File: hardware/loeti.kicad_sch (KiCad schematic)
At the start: 101 parts, among them J1 REDFIT_SWD_6, J2 POWER, J3 DEBUG, Q1 Si4162DY, Q2 BC817, Q3 Si4425FDY, Q4 BC817, Q5 BC807, SW1 BOOT, SW3 RotaryEncoder_Switch, U10 TPS62177DQC, U2 EA_OLEDS102-6, U3 M24C64-RMN, U4 STM32G431CBTx, U5 TCPP01-M12, U6 74AHC1G08, U7 USBLC6-2SC6, U8 TLV333-DBV, U9 INA301A1

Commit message: chore: update PCB design
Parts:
- removed D3: BAT54S, Package_TO_SOT_SMD:SOT-23, symbol Diode:BAT54S
- removed R10, R8: 10k, Resistor_SMD:R_0603_1608Metric, symbol Device:R
- removed TP1: 1C, Connector_Wire:SolderWire-0.75sqmm_1x01_D1.25mm_OD2.3mm, symbol Connector:TestPoint
- removed TP2: 3P, Connector_Wire:SolderWire-0.75sqmm_1x01_D1.25mm_OD2.3mm, symbol Connector:TestPoint
- removed TP3: 2T, Connector_Wire:SolderWire-0.75sqmm_1x01_D1.25mm_OD2.3mm, symbol Connector:TestPoint
- removed TP4: 4D, Connector_Wire:SolderWire-0.75sqmm_1x01_D1.25mm_OD2.3mm, symbol Connector:TestPoint
- removed TP5: 5S, Connector_Wire:SolderWire-0.75sqmm_1x01_D1.25mm_OD2.3mm, symbol Connector:TestPoint
- added J4: XLR4, custom:MiniXLR-4_Switchcraft_TRAPCS_Horizontal, symbol Connector_Audio:XLR4
- added U1: LMR33610ADDAR, Package_SO:Texas_HSOP-8-1EP_3.9x4.9mm_P1.27mm_ThermalVias, symbol Regulator_Switching:LMR33610ADDAR
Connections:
- net DET: now also J4.2
- net GND: now also J4.4
- net HEATER: now also J4.3
- net TC+: now also J4.1
- net _SLEEP: no longer names the net of U4.22 (PB10)
- new net: U1.1 (GND), U1.9 (GND)
- no-connect marks 21 -> 22
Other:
- note added: "Det can be used for sleep sensing (pull to GND)"
- note removed: "VOGT 1018.68"
- moved on the sheet: D4, R11, R9

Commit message: chore: generate production outputs
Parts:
- removed J1: REDFIT_SWD_6, connectors-debug:WR-WST REDFIT IDC 6 DBG, symbol Connectors_Debug:REDFIT_SWD_6
- removed U1: LMR33610ADDAR, Package_SO:Texas_HSOP-8-1EP_3.9x4.9mm_P1.27mm_ThermalVias, symbol Regulator_Switching:LMR33610ADDAR
- added J1: REDFIT_SWD_6, connectors-debug:WR-WST REDFIT IDC 6 DBG, symbol connectors-debug:REDFIT_SWD_6
- C27: renamed from C33; value DNP -> ~; MPN C14663 -> (none); now not fitted
- J2: renamed from J3; JLCPCB Position Offset 0,1.335 -> (none)
- J3: renamed from J2; JLCPCB Position Offset 0,1.335 -> (none)
- U5: MPN (none) -> C1121848
- U7: renamed from U8; footprint Package_TO_SOT_SMD:SOT-23-5 -> Package_TO_SOT_SMD:SOT-23-5_HandSoldering
- U8: renamed from U9; MPN (none) -> C471062
- U9: renamed from U10; MPN (none) -> C91241
- renumbered C11 to C10, C12 to C11, C27 to C12, C28 to C13, C16 to C14, C17 to C15, C18 to C16, C19 to C17, C13 to C18, C14 to C19, C4 to C2, C25 to C23, C26 to C24, C15 to C25, C32 to C26, C23 to C28, C24 to C29, C5 to C3, C34 to C30, C35 to C31, C30 to C32, C31 to C33, C6 to C4, C7 to C5, C2 to C6, C3 to C7, C9 to C8, C10 to C9, D4 to D1, D1 to D2, D2 to D3, D6 to D4, D7 to D5, D5 to D6, D9 to D7, R33 to R1, R15 to R10, R16 to R11, R17 to R12, R18 to R13, R19 to R14, R7 to R15, R21 to R16, R12 to R17, R23 to R18, R13 to R19, R34 to R2, R24 to R20, R25 to R21, R26 to R22, R27 to R23, R20 to R24, R28 to R25, R22 to R26, R29 to R27, R30 to R28, R31 to R29, R32 to R30, R9 to R7, R11 to R8, R14 to R9, SW3 to SW2, U7 to U1
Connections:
- net +3V3: now also J1.1 (VREF)
- net GND: now also J1.5 (GND)
- net NRST: now also J1.3 (nRST)
- net SWO: now also J1.6 (SWO)
- net TCK: now also J1.4 (SWCLK)
- net TMS: now also J1.2 (SWDIO)
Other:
- moved on the sheet: C12, C13, C6, C7, FB1, R5, U4

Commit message: fix: hardware issues
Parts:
- removed D5: BAT54S, Package_TO_SOT_SMD:SOT-23, symbol Diode:BAT54S
- J4: value XLR4 -> TRAPC4MSX
- L1: value 10u -> LMDND4040WKT100MM
- U7: footprint Package_TO_SOT_SMD:SOT-23-5_HandSoldering -> Package_TO_SOT_SMD:SOT-23-5
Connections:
- net DET: now also J4.4; no longer J4.2
- net GND: now also J4.1; no longer J4.4
- net HEATER: now also J4.2; no longer J4.3
- net TC+: now also J4.3; no longer J4.1
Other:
- moved on the sheet: C32, C33, D7, D8, L1, U9

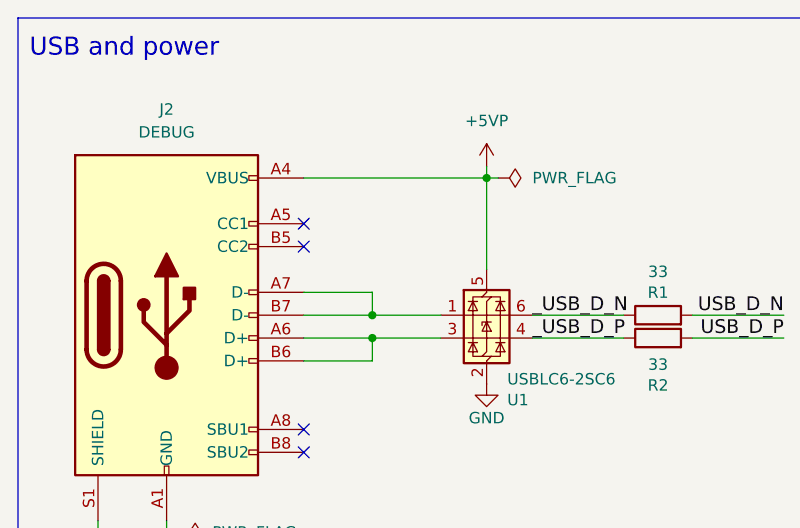
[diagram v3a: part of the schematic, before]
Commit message: fix: pcb for minor mistakes
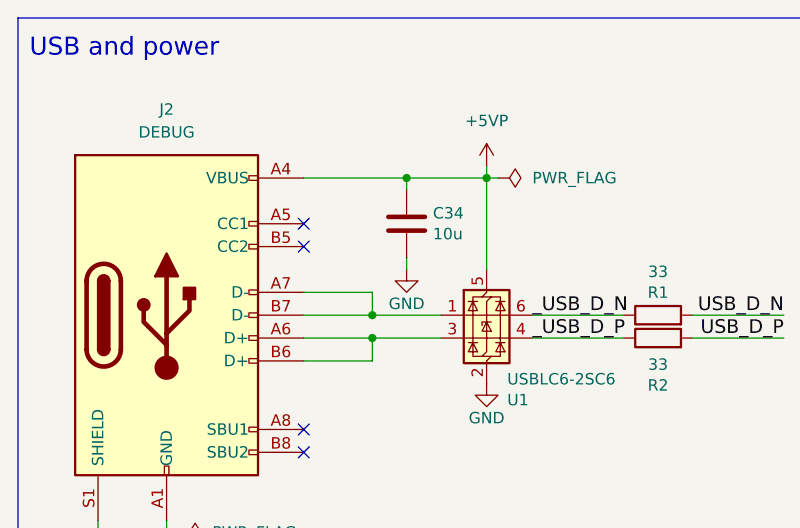
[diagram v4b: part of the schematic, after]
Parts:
- added C34: 10u, Capacitor_SMD:C_1206_3216Metric, symbol Device:C
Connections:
- net +5VP: now also C34.1
- net GND: now also C34.2
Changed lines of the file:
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@@
 	(title_block
 		(title "loeti v6")
-		(date "2025-06-18")
+		(date "2025-07-01")
 		(rev "c")
 		(company "elagil")
@@
 	)
 	(junction
+		(at 59.69 30.48)
+		(diameter 0)
+		(color 0 0 0 0)
+	)
+	(junction
 		(at 364.49 177.8)
 		(diameter 0)
@@
 	(wire
 		(pts
+			(xy 59.69 30.48) (xy 59.69 31.75)
+		)
+		(stroke
+			(width 0)
+			(type default)
+		)
+	)
+	(wire
+		(pts
 			(xy 35.56 161.29) (xy 35.56 168.91)
 		)
@@
 	(wire
 		(pts
+			(xy 59.69 39.37) (xy 59.69 40.64)
+		)
+		(stroke
+			(width 0)
+			(type default)
+		)
+	)
+	(wire
+		(pts
 			(xy 82.55 168.91) (xy 95.25 168.91)
 		)
@@
 	(wire
 		(pts
+			(xy 59.69 30.48) (xy 68.58 30.48)
+		)
+		(stroke
+			(width 0)
+			(type default)
+		)
+	)
+	(wire
+		(pts
 			(xy 132.08 40.64) (xy 146.05 40.64)
 		)
@@
 	(wire
 		(pts
-			(xy 48.26 30.48) (xy 68.58 30.48)
+			(xy 48.26 30.48) (xy 59.69 30.48)
 		)
 		(stroke
@@
 	(symbol
 		(lib_id "Device:C")
+		(at 59.69 35.56 0)
+		(unit 1)
+		(exclude_from_sim no)
+		(in_bom yes)
+		(on_board yes)
+		(dnp no)
+		(property "Reference" "C34"
+			(at 62.611 34.3916 0)
+			(effects
+				(font
+					(size 1.27 1.27)
+				)
+				(justify left)
+			)
+		)
+		(property "Value" "10u"
+			(at 62.611 36.703 0)
+			(effects
+				(font
+					(size 1.27 1.27)
+				)
+				(justify left)
+			)
+		)
+		(property "Footprint" "Capacitor_SMD:C_1206_3216Metric"
+			(at 60.6552 39.37 0)
+			(effects
+				(font
+					(size 1.27 1.27)
+				)
+				(hide yes)
+			)
+		)
+		(property "Datasheet" "~"
+			(at 59.69 35.56 0)
+			(effects
+				(font
+					(size 1.27 1.27)
+				)
+				(hide yes)
+			)
+		)
+		(property "Description" "Unpolarized capacitor"
+			(at 59.69 35.56 0)
+			(effects
+				(font
+					(size 1.27 1.27)
+				)
+				(hide yes)
+			)
+		)
+		(property "Mfr.Nr." ""
+			(at 59.69 35.56 0)
+			(effects
+				(font
+					(size 1.27 1.27)
+				)
+				(hide yes)
+			)
+		)
+		(property "MPN" "C13585"
+			(at 59.69 35.56 0)
+			(effects
+				(font
+					(size 1.27 1.27)
+				)
+				(hide yes)
+			)
+		)
+		(property "JLCPCB Position Offset" ""
+			(at 59.69 35.56 0)
+			(effects
+				(font
+					(size 1.27 1.27)
+				)
+				(hide yes)
+			)
+		)
+		(property "Sim.Library" ""
+			(at 59.69 35.56 0)
+			(effects
+				(font
+					(size 1.27 1.27)
+				)
+				(hide yes)
+			)
+		)
+		(property "Sim.Name" ""
+			(at 59.69 35.56 0)
+			(effects
+				(font
+					(size 1.27 1.27)
+				)
+				(hide yes)
+			)
+		)
+		(pin "1"
+		)
+		(pin "2"
+		)
+		(instances
+			(project "loeti"
+				(path "/e4270527-a28c-4130-b442-7148380c12e2"
+					(reference "C34")
+					(unit 1)
+				)
+			)
+		)
+	)
+	(symbol
+		(lib_id "Device:C")
 		(at 242.57 86.36 180)
 		(unit 1)
@@
 					(unit 1)
 				)
+			)
+		)
+	)
+	(symbol
+		(lib_id "power:GND")
+		(at 59.69 40.64 0)
+		(unit 1)
+		(exclude_from_sim no)
+		(in_bom yes)
+		(on_board yes)
+		(dnp no)
+		(property "Reference" "#PWR032"
+			(at 59.69 46.99 0)
+			(effects
+				(font
+					(size 1.27 1.27)
+				)
+				(hide yes)
+			)
+		)
+		(property "Value" "GND"
+			(at 59.69 44.45 0)
+			(effects
+				(font
+					(size 1.27 1.27)
+				)
+			)
+		)
+		(property "Footprint" ""
+			(at 59.69 40.64 0)
+			(effects
+				(font
+					(size 1.27 1.27)
+				)
+				(hide yes)
+			)
+		)
+		(property "Datasheet" ""
+			(at 59.69 40.64 0)
+			(effects
+				(font
+					(size 1.27 1.27)
+				)
+				(hide yes)
+			)
+		)
+		(property "Description" "Power symbol creates a global label with name \"GND\" , ground"
+			(at 59.69 40.64 0)
+			(effects
+				(font
+					(size 1.27 1.27)
+				)
+				(hide yes)
+			)
+		)
+		(pin "1"
+		)
+		(instances
+			(project "loeti"
+				(path "/e4270527-a28c-4130-b442-7148380c12e2"
+					(reference "#PWR032")
+					(unit 1)
+				)

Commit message: feat: holder
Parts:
- removed J4: TRAPC4MSX, custom:MiniXLR-4_Switchcraft_TRAPCS_Horizontal, symbol Connector_Audio:XLR4
- added C35: 22p, Capacitor_SMD:C_0603_1608Metric, symbol Device:C
- added D5: B5819W SL, Diode_SMD:D_SOD-123, symbol Device:D_Schottky
- added J4: Conn_01x04_Pin, Connector_PinHeader_2.54mm:PinHeader_1x04_P2.54mm_Horizontal, symbol Connector:Conn_01x04_Pin
- added L2: LMDND4040WKT100MM, Inductor_SMD:L_Abracon_ASPI-0425, symbol Device:L
- added R31: 220k, Resistor_SMD:R_0603_1608Metric, symbol Device:R
- added R32: 2M, Resistor_SMD:R_0603_1608Metric, symbol Device:R
- added TP1: GND, Connector_PinSocket_2.54mm:PinSocket_1x01_P2.54mm_Vertical, symbol Connector:TestPoint
- added TP2: DET, Connector_PinSocket_2.54mm:PinSocket_1x01_P2.54mm_Vertical, symbol Connector:TestPoint
- added TP3: TC+, Connector_PinSocket_2.54mm:PinSocket_1x01_P2.54mm_Vertical, symbol Connector:TestPoint
- added TP4: HEATER, Connector_PinSocket_2.54mm:PinSocket_1x01_P2.54mm_Vertical, symbol Connector:TestPoint
- added TP5: HEATER, TestPoint:TestPoint_THTPad_2.5x2.5mm_Drill1.2mm, symbol Connector:TestPoint
- added TP6: DET, TestPoint:TestPoint_THTPad_2.5x2.5mm_Drill1.2mm, symbol Connector:TestPoint
- added TP7: TC+, TestPoint:TestPoint_THTPad_2.5x2.5mm_Drill1.2mm, symbol Connector:TestPoint
- added TP8: GND, TestPoint:TestPoint_THTPad_2.5x2.5mm_Drill1.2mm, symbol Connector:TestPoint
- added U10: TPS61040DBV, Package_TO_SOT_SMD:SOT-23-5, symbol Regulator_Switching:TPS61040DBV
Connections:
- net +3V3: now also L2.1, U10.4 (EN), U10.5 (VIN)
- net DET: now also J4.1 (Pin_1)
- net GND: now also J4.3 (Pin_3), R31.2, U10.2 (GND)
- net HEATER: now also J4.4 (Pin_4)
- net OLED_VCC: now also C35.1, D5.1 (K), R32.1
- net TC+: now also J4.2 (Pin_2)
- new net: C35.2, R31.1, R32.2, U10.3 (FB)
- new net: D5.2 (A), L2.2, U10.1 (SW)
- new net DET_SEC: TP2.1, TP6.1
- new net GND_SEC: TP1.1, TP8.1
- new net HEATER_SEC: TP4.1, TP5.1
- new net TC+_SEC: TP3.1, TP7.1
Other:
- moved on the sheet: C18, C19, C23, C24, C25, C28, C29, C32, C33, C34, C6, C7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

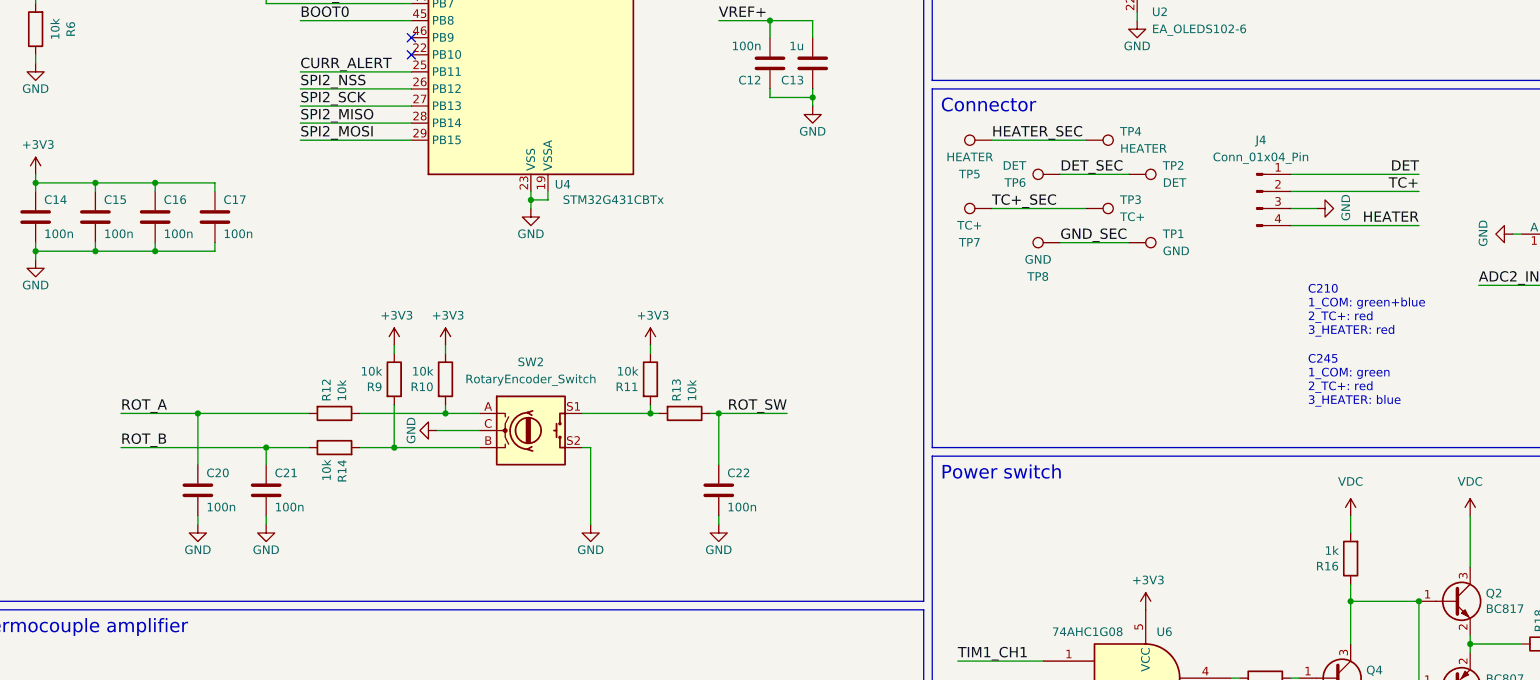
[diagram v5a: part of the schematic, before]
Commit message: feat: hardware modules for new XLR connector
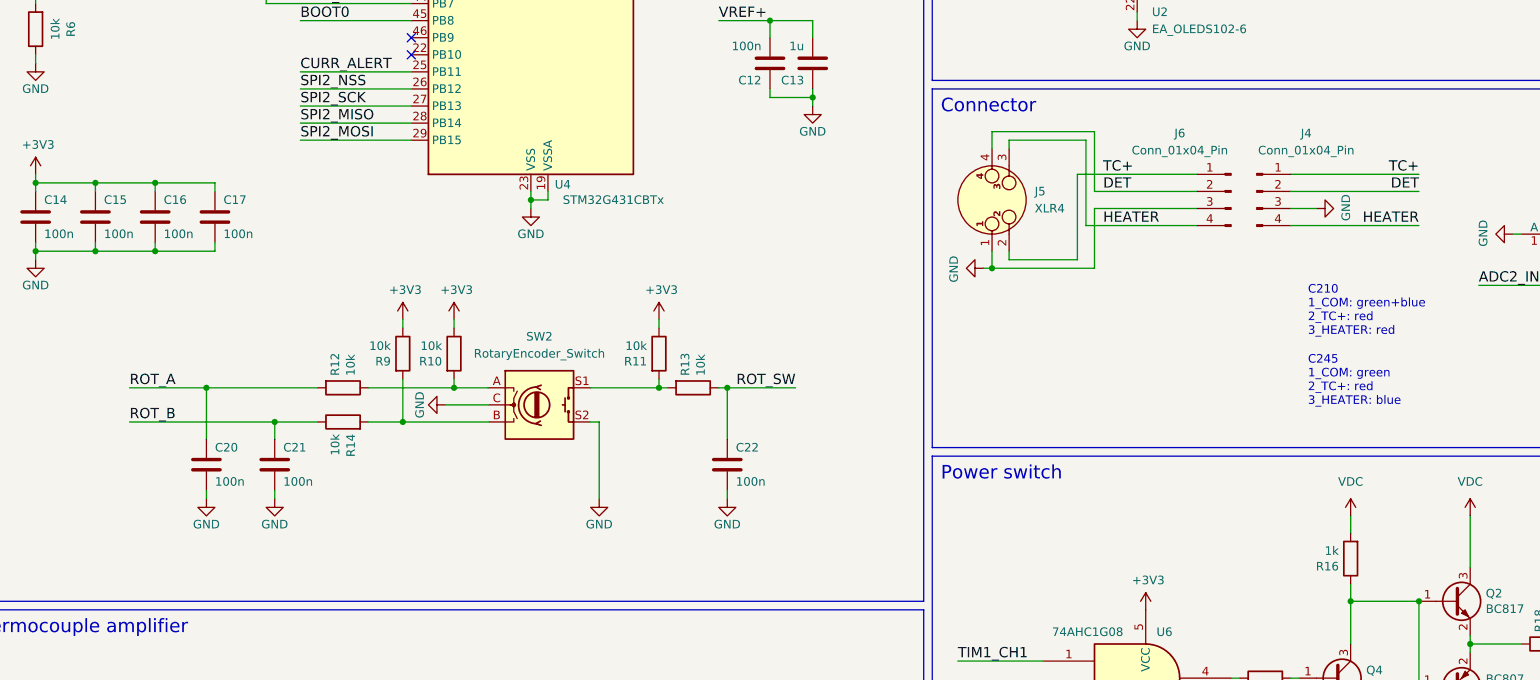
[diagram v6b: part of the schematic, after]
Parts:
- removed TP1: GND, Connector_PinSocket_2.54mm:PinSocket_1x01_P2.54mm_Vertical, symbol Connector:TestPoint
- removed TP2: DET, Connector_PinSocket_2.54mm:PinSocket_1x01_P2.54mm_Vertical, symbol Connector:TestPoint
- removed TP3: TC+, Connector_PinSocket_2.54mm:PinSocket_1x01_P2.54mm_Vertical, symbol Connector:TestPoint
- removed TP4: HEATER, Connector_PinSocket_2.54mm:PinSocket_1x01_P2.54mm_Vertical, symbol Connector:TestPoint
- removed TP5: HEATER, TestPoint:TestPoint_THTPad_2.5x2.5mm_Drill1.2mm, symbol Connector:TestPoint
- removed TP6: DET, TestPoint:TestPoint_THTPad_2.5x2.5mm_Drill1.2mm, symbol Connector:TestPoint
- removed TP7: TC+, TestPoint:TestPoint_THTPad_2.5x2.5mm_Drill1.2mm, symbol Connector:TestPoint
- removed TP8: GND, TestPoint:TestPoint_THTPad_2.5x2.5mm_Drill1.2mm, symbol Connector:TestPoint
- added J5: XLR4, custom:MiniXLR-4_Rean_RT4MPR, symbol Connector_Audio:XLR4
- added J6: Conn_01x04_Pin, Connector_PinHeader_2.54mm:PinHeader_1x04_P2.54mm_Vertical, symbol Connector:Conn_01x04_Pin
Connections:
- net DET: now also J4.2 (Pin_2), J5.4, J6.2 (Pin_2); no longer J4.1 (Pin_1)
- net GND: now also J5.1, J6.3 (Pin_3)
- net HEATER: now also J5.3, J6.4 (Pin_4)
- net TC+: now also J4.1 (Pin_1), J5.2, J6.1 (Pin_1); no longer J4.2 (Pin_2)
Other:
- moved on the sheet: C20, C21, C22, R10, R11, R12, R13, R14, R9, SW2
